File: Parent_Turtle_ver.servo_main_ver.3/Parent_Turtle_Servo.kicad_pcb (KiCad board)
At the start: 2 copper layers, 70 x 60 mm, 55 parts, among them P1 CONN_02X15, P10 WRITING, P11 A/D, P12 5V_in, P13 CONN_02X04, P14 I/O, P15 CONN_02X04, P2 CONN_02X15, P3 CAN, P4 CAN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

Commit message: Increase pwm-pins
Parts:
- added D12: DIODE, Mizz_lib:SOD-123, B.Cu at (125.5, 85.8)
- added P16: PWM, Pin_Headers:Pin_Header_Straight_1x02, F.Cu at (153.2, 81.8)
- P5: footprint Pin_Headers:Pin_Header_Straight_1x12 -> Pin_Headers:Pin_Header_Straight_1x14
- moved SP1 2.04 mm to (125.0, 91.0)
- moved P5 1.59 mm to (104.8, 89.5)
- moved P12 0.89 mm to (151.8, 75.5)
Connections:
- P5 pad 1: /A1 -> /E6
- P5 pad 10: /E11 -> /B0
- P5 pad 11: /E13 -> /E9
- P5 pad 12: /E14 -> /E11
- P5 pad 2: /A0 -> /E5
- P5 pad 3: /A3 -> /A1
- P5 pad 4: /A2 -> /A0
- P5 pad 5: /A7 -> /A3
- P5 pad 6: /A6 -> /A2
- P5 pad 7: /B1 -> /A7
- P5 pad 8: /B0 -> /A6
- P5 pad 9: /E9 -> /B1
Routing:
- net /C9: track 0.00 -> 28.9 mm
- net /E5: track 0.00 -> 20.0 mm
- net /E6: track 0.00 -> 19.4 mm
- net /B8: track 0.00 -> 10.7 mm
- net /E9: track 8.49 -> 11.5 mm
- net /E13: track 8.49 -> 11.5 mm
- net /E14: track 11.0 -> 14.1 mm
- net /A6: track 11.0 -> 14.1 mm
- net /B1: track 7.44 -> 10.5 mm
- net /A3: track 7.44 -> 10.5 mm
- net /A2: track 11.0 -> 14.1 mm
- net /B0: track 11.0 -> 14.1 mm
- net /E11: track 8.51 -> 11.5 mm
- net /A7: track 7.46 -> 10.5 mm
- net +5V: track 162.7 -> 165.4 mm
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
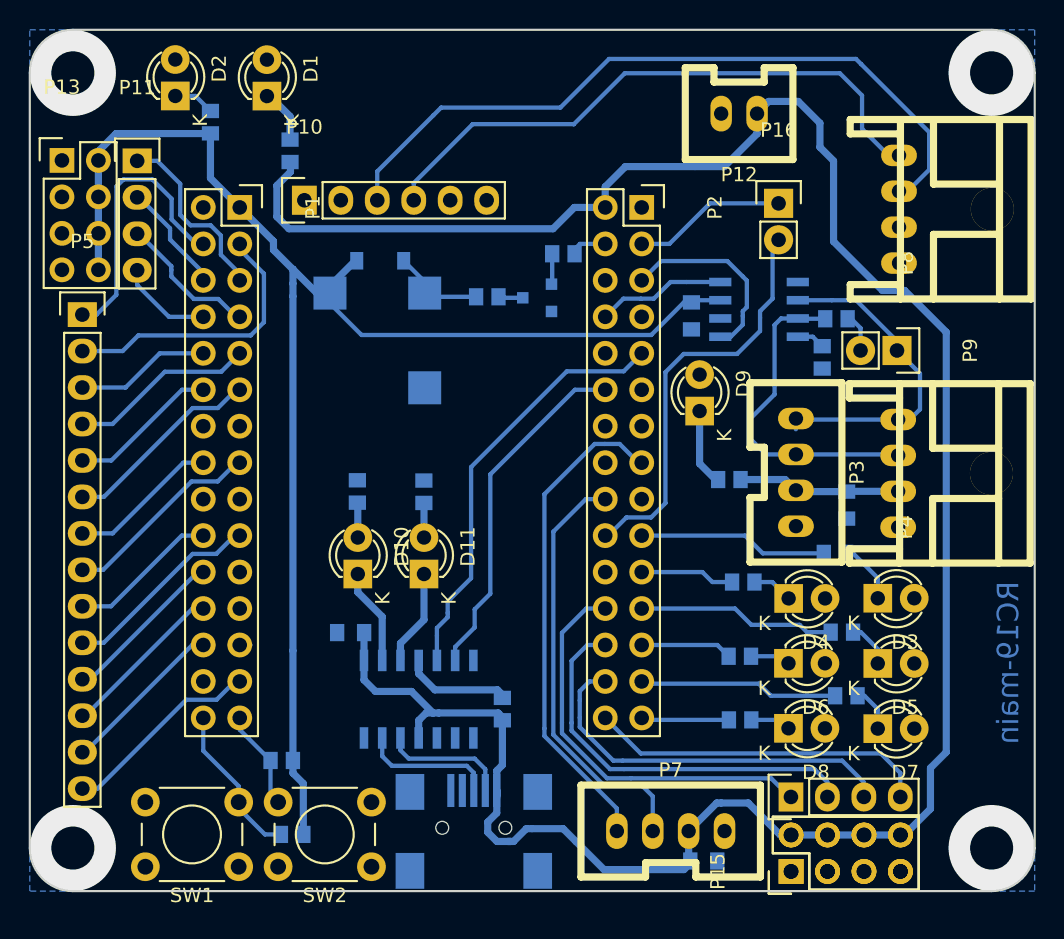
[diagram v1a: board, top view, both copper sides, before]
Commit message: シリアル2まで追加
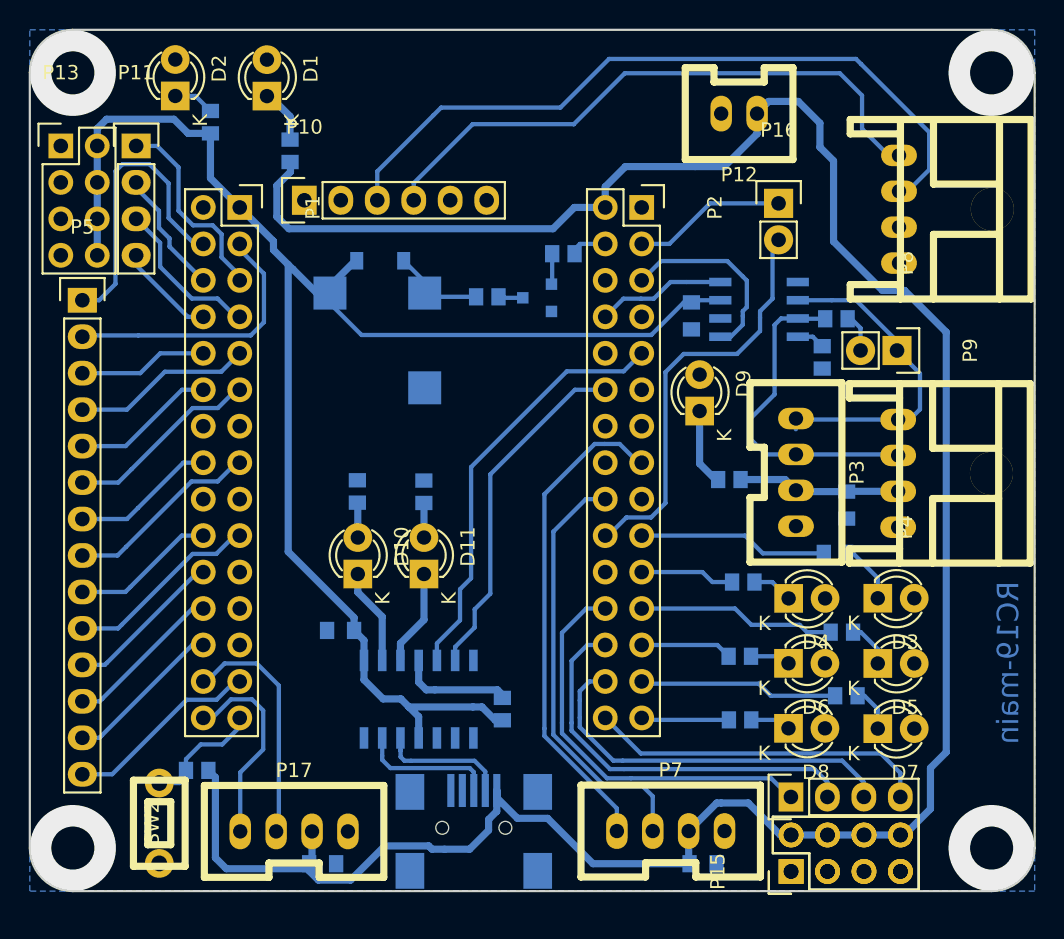
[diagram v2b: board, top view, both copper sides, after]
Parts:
- removed R2: 10k, Resistors_SMD:R_0603
- removed SW1: SW_PUSH, Buttons_Switches_ThroughHole:SW_PUSH_6mm
- added C5: 0.1u, Capacitors_SMD:C_0603, B.Cu at (121.5, 127.8)
- added P17: SERIAL2, RP_KiCAD_Connector:XA_4T, F.Cu at (115.8, 125.5)
- SW2: footprint Buttons_Switches_ThroughHole:SW_PUSH_6mm -> Mizz_lib:RP_TroughHole_Button
- moved C2 29.9 mm to (122.8, 111.5), turned to 0 degrees
- moved C3 29.4 mm to (148.0, 127.8), turned to 0 degrees
- moved SW2 15.1 mm to (110.1, 124.9), turned to 270 degrees
- moved R7 5.93 mm to (112.8, 121.2)
- moved P11 1.04 mm to (108.5, 77.8)
- moved P13 1.01 mm to (103.2, 77.8)
- moved P5 1.00 mm to (104.8, 88.5)
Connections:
- C2 pad 2: +5V -> +3.3V
- R18 pad 2: +5V -> +3.3V
- R7 pad 1: +3.3V -> +5V
- U2 pad 1: +5V -> +3.3V
- U2 pad 11: +5V -> +3.3V
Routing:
- net /B10: track 0.00 -> 16.7 mm
- net +5V: track 165.4 -> 173.5 mm
- net +3.3V: track 104.7 -> 110.4 mm
- net /B11: track 11.0 -> 14.1 mm
- net /B13: track 6.97 -> 8.57 mm
- net /E6: track 19.4 -> 20.7 mm
- net /C1: track 7.77 -> 8.76 mm
- net /E12: track 0.75 -> 0.00 mm
- net /C0: track 13.4 -> 14.0 mm

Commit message: シリアルの番号の整理
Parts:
- P17: value SERIAL2 -> SERIAL0
- P6: value USB_OTG -> SERIAL1
- P7: value SERIAL1 -> SERIAL2
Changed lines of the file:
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@@
   )
   (setup
-    (last_trace_width 0.5)
+    (last_trace_width 0.25)
     (user_trace_width 0.3)
     (user_trace_width 0.5)
@@
       (effects (font (size 1 1) (thickness 0.15)))
     )
-    (fp_text value SERIAL1 (at 0 -0.5) (layer F.Fab)
+    (fp_text value SERIAL2 (at 0 -0.5) (layer F.Fab)
       (effects (font (size 1 1) (thickness 0.15)))
     )
@@
       (effects (font (size 1 1) (thickness 0.15)) (justify mirror))
     )
-    (fp_text value USB_OTG (at 0 7.0993 90) (layer B.Fab)
+    (fp_text value SERIAL1 (at 0 7.0993 90) (layer B.Fab)
       (effects (font (size 1 1) (thickness 0.15)) (justify mirror))
     )
@@
       (effects (font (size 1 1) (thickness 0.15)))
     )
-    (fp_text value SERIAL2 (at 0 -0.5) (layer F.Fab)
-      (effects (font (size 1 1) (thickness 0.15)))
-    )
+    (fp_text value SERIAL0 (at 0 -0.5) (layer F.Fab)
+      (effects (font (size 1 1) (thickness 0.15)))
+    )

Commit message: main基板最終版
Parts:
- removed the P15 at (154.1, 128.3)
- added C6: 0.1u, Capacitors_SMD:C_0603, B.Cu at (165.8, 105.2)
- added C7: 0.1u, Capacitors_SMD:C_0603, B.Cu at (168.9, 114.6)
- added R2: 10k, Resistors_SMD:R_0603, B.Cu at (124.0, 125.5)
- added SW1: SW1, Mizz_lib:RP_TroughHole_Button, F.Cu at (124.2, 127.0)
- added U3: 78L05, TO_SOT_Packages_SMD:SOT89-3_Housing, B.Cu at (166.6, 109.4)
- D10, D11: footprint LEDs:LED-3MM -> LEDs:LED_0603; moved to B.Cu
- SW2: value SW_PUSH -> SW0
- moved SW2 14.3 mm to (124.2, 122.8), turned to 0 degrees
- moved R7 11.5 mm to (124.0, 123.8)
- moved P17 5.75 mm to (110.0, 125.5)
- moved P16 5.55 mm to (147.8, 82.5), turned to 90 degrees
- moved C5 5.26 mm to (116.2, 127.5)
- moved P6 1.99 mm to (134.0, 126.2)
- moved D10 1.32 mm to (124.0, 106.2), turned to 270 degrees
- moved D11 1.32 mm to (128.5, 106.2), turned to 270 degrees
- moved C3 1.00 mm to (149.0, 127.8)
- moved R18 0.98 mm to (134.0, 116.0)
- moved P7 0.76 mm to (142.8, 125.5)
- moved P14 0.65 mm to (154.8, 123.0)
- moved P15 0.63 mm to (154.8, 128.2)
- moved U2 0.30 mm to (128.2, 116.0)
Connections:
- R7 pad 2: /B13 -> /E10
- SW2 pad 2: /B13 -> /E10
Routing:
- net /E12: track 0.00 -> 20.1 mm
- net /E10: track 0.00 -> 18.0 mm
- net +12V: track 11.3 -> 19.7 mm
- net /B13: track 8.57 -> 0.63 mm
- net /B8: track 10.7 -> 4.89 mm
- net /B11: track 14.1 -> 9.22 mm
- net /A9: track 30.9 -> 27.9 mm
- net /C9: track 28.9 -> 31.3 mm
- net /D+: track 9.54 -> 11.5 mm
- net /D-: track 8.97 -> 10.8 mm
- net +5V: track 173.5 -> 171.7 mm
- net /B10: track 16.7 -> 17.7 mm
- net +3.3V: track 110.4 -> 109.5 mm
- net /D13: track 28.0 -> 27.2 mm
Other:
- board text removed: "RC19-main"
